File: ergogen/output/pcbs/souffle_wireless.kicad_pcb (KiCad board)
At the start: 2 copper layers, 134.9 x 109.8 mm, 128 parts

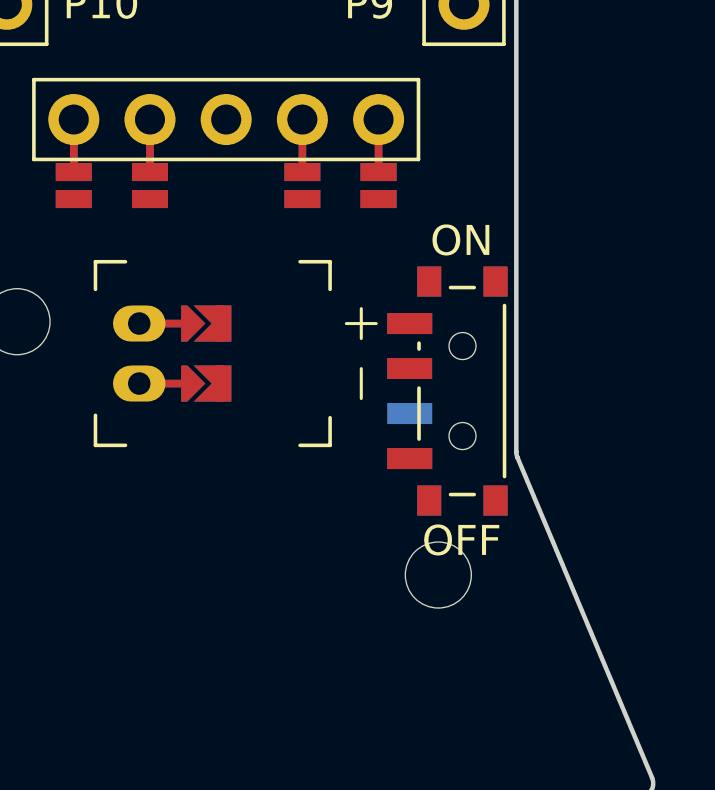
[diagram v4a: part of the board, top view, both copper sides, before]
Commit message: feat: adjusted the screw hole instead
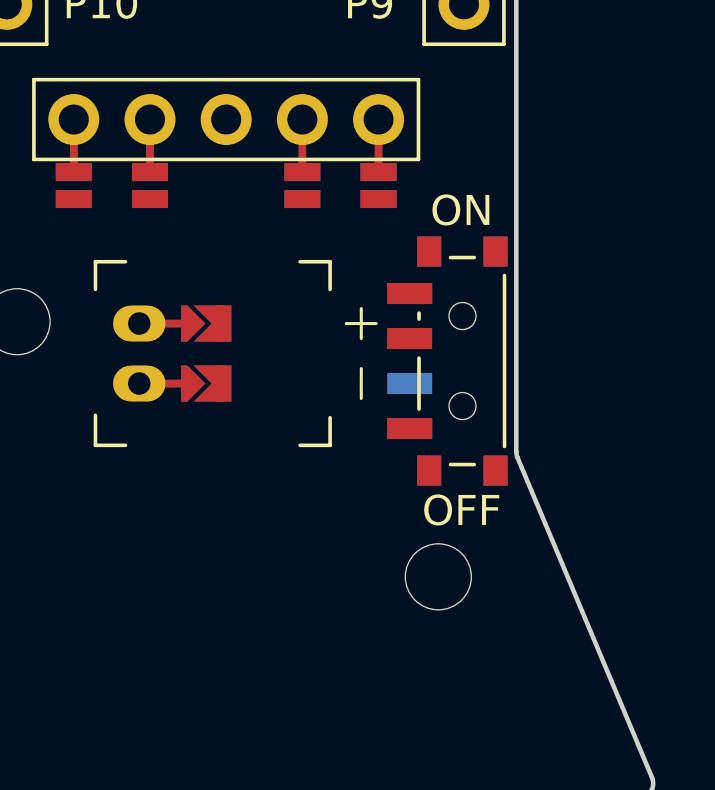
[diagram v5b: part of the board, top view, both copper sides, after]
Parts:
- moved PWR1 1.00 mm to (219.8, 101.8)
- moved MH2 0.06 mm to (219.0, 108.9)
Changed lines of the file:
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@@
   (footprint "ceoloide:mounting_hole_npth"
     (layer "F.Cu")
-    (at 218.969 108.8825 0)
+    (at 218.969 108.9425 0)
     (property "Reference" "MH2"
       (at 0 2.55 0)
@@
   (footprint "ceoloide:power_switch_smd_side"
     (layer "F.Cu")
-    (at 219.75 102.75 0)
+    (at 219.75 101.75 0)
     (property "Reference" "PWR1"
       (at -3.6 0 -90)
